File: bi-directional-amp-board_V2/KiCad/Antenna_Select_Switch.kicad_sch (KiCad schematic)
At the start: 17 parts

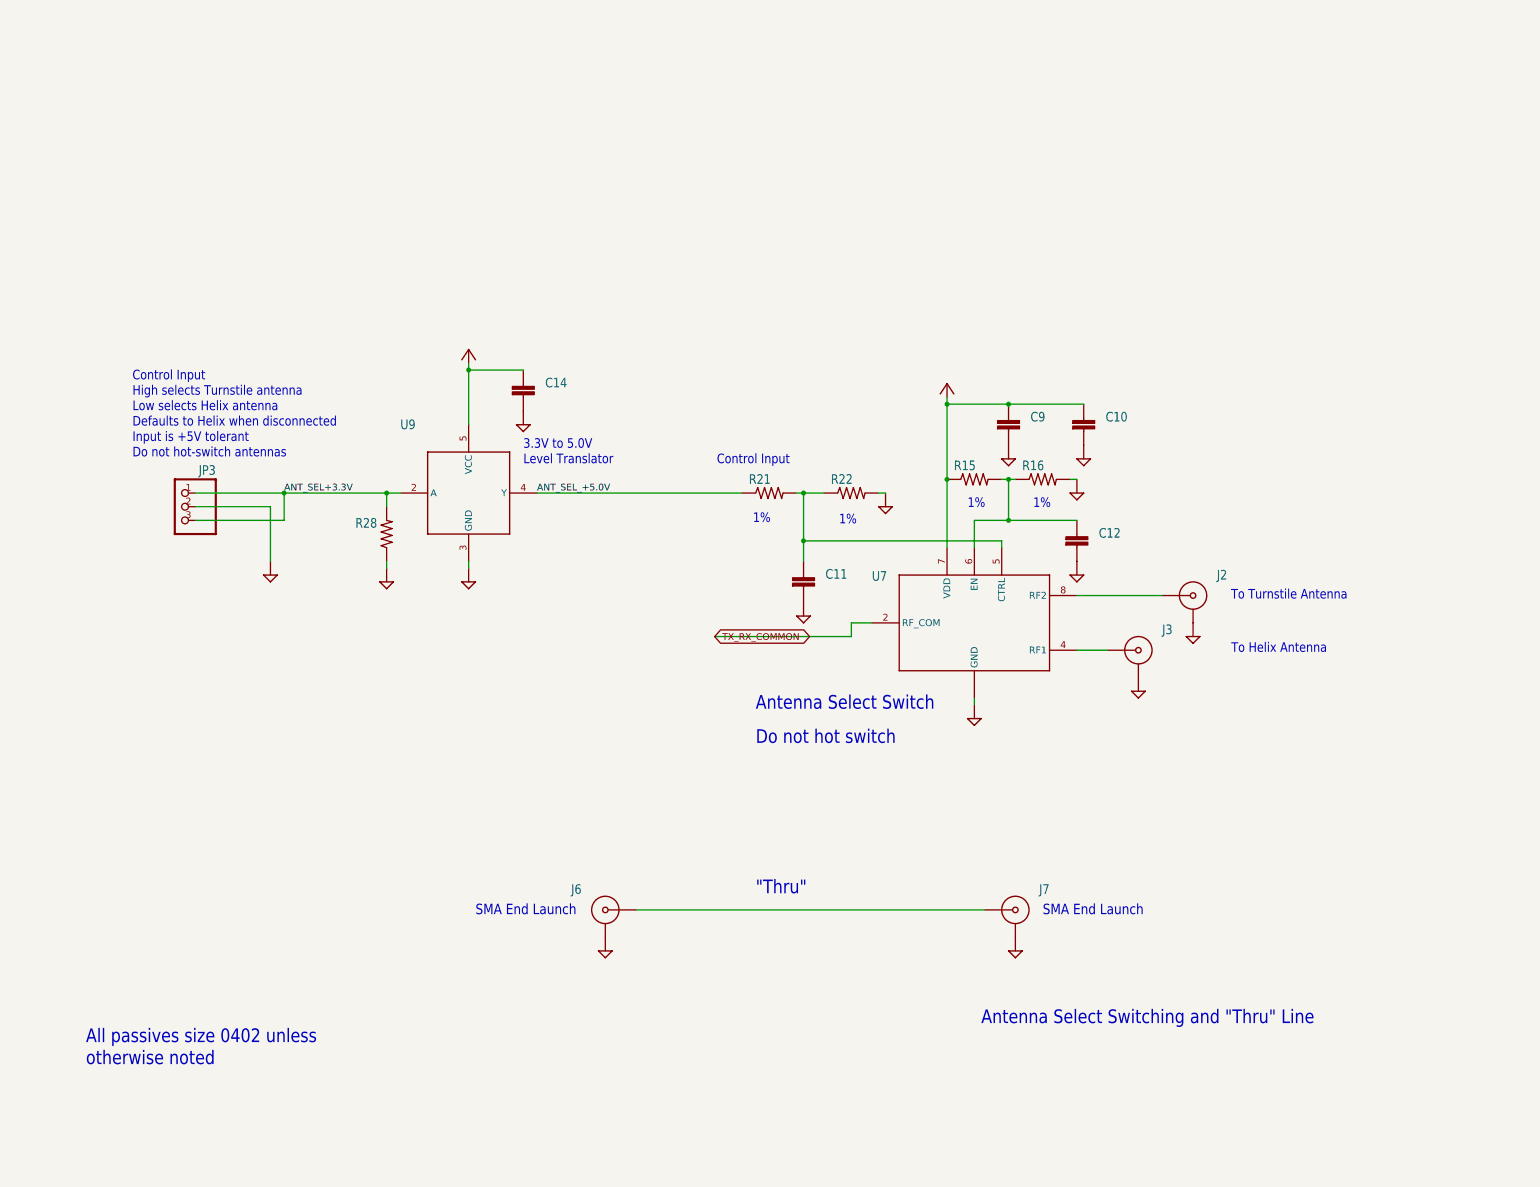
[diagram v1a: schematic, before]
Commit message: Updated KiCAD import of bidirectional amplifier. Still a bit broken, but better now.
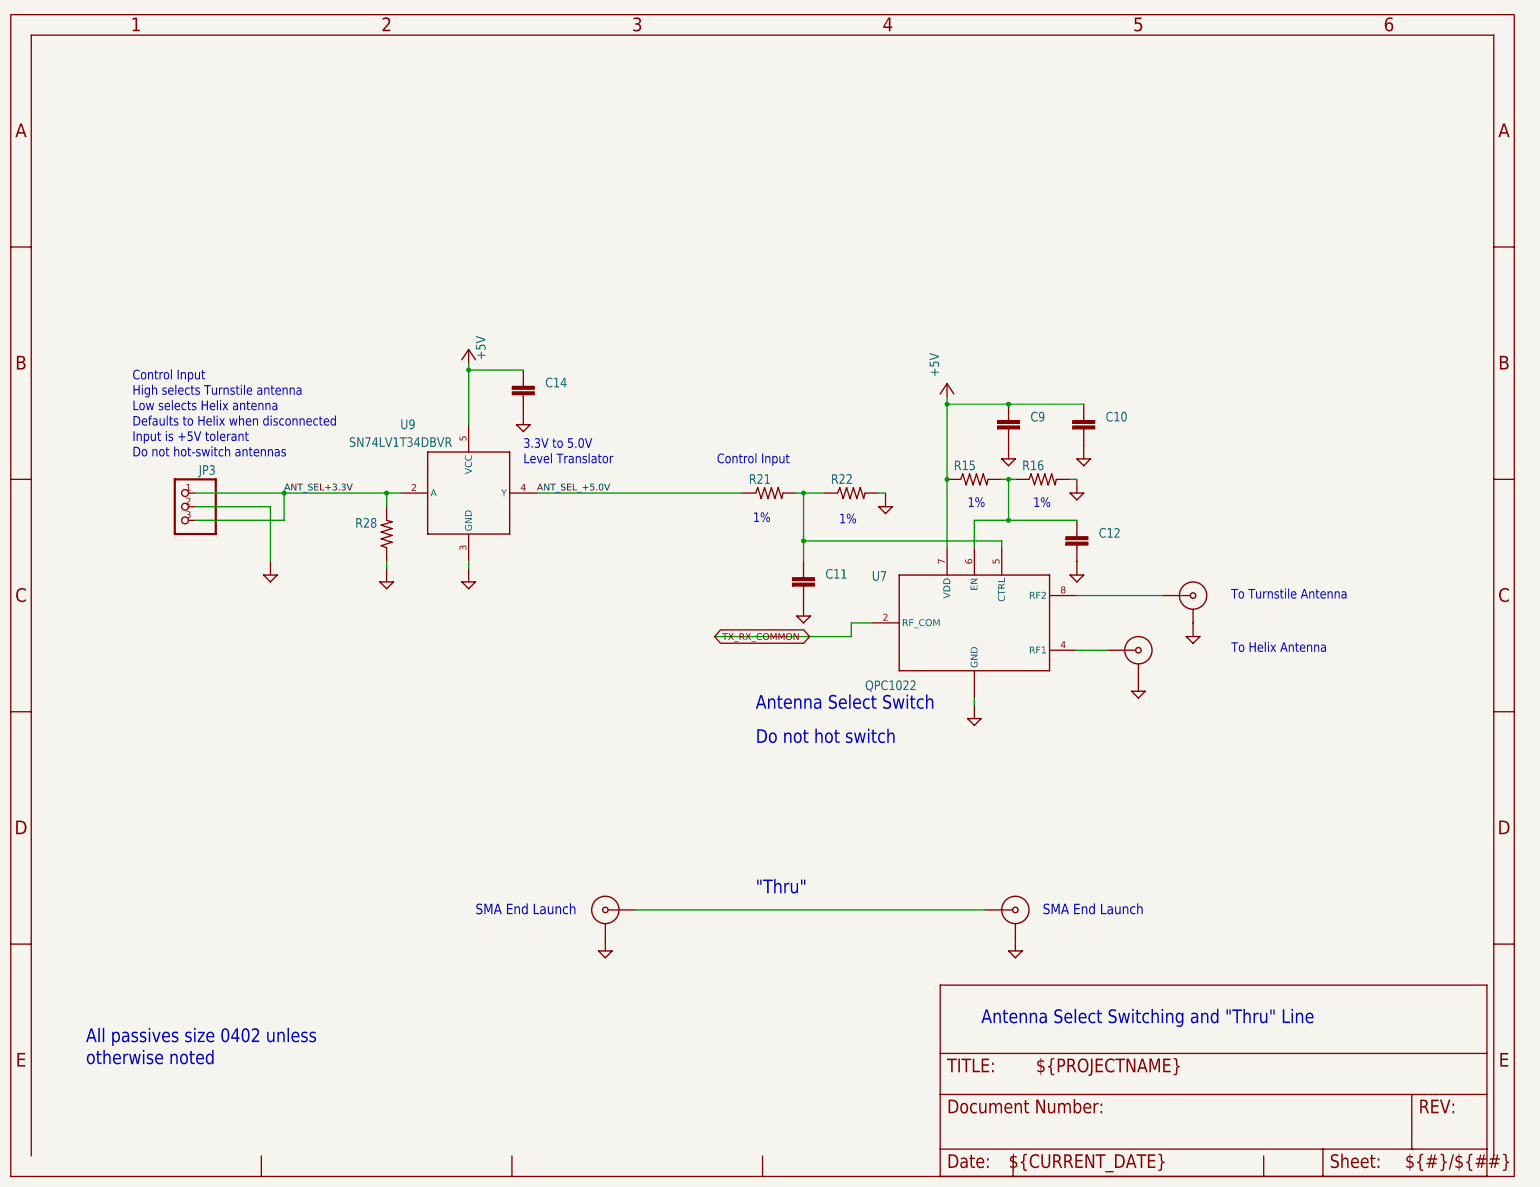
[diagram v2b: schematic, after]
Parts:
- C10, C14: value (none) -> C-EU0402-B-NOSILK; footprint (none) -> Bidirectional_Amp:.0402-B-NOSILK; MFR (none) -> TDK Corporation; MPN (none) -> CGA2B1X7R1C104K050BC
- C11, C12: value (none) -> C-EU0402-B-NOSILK; footprint (none) -> Bidirectional_Amp:.0402-B-NOSILK; MPN (none) -> GCM1555C1H101JA16D
- C9: value (none) -> C-EU0402-B-NOSILK; footprint (none) -> Bidirectional_Amp:.0402-B-NOSILK; MFR (none) -> Murata; MPN (none) -> GCM1555C1H101JA16D
- J2, J3, J6, J7: value (none) -> 142-0701-851_ALT; footprint (none) -> Bidirectional_Amp:142-0701-851; MFR (none) -> Cinch; MPN (none) -> 142-0701-851
- JP3: value (none) -> PINHD-1X3; footprint (none) -> Bidirectional_Amp:1X03; MFR (none) -> Molex; MPN (none) -> 22-23-2031
- R15, R21: value (none) -> R-US_0402-B-NOSILK; footprint (none) -> Bidirectional_Amp:.0402-B-NOSILK; MFR (none) -> Panasonic; MPN (none) -> ERJ-2RKF1002X
- R16, R22: value (none) -> R-US_0402-B-NOSILK; footprint (none) -> Bidirectional_Amp:.0402-B-NOSILK; MFR (none) -> Panasonic; MPN (none) -> ERJ-2RKF5621X
- R28: value (none) -> R-US_0402-B-NOSILK; footprint (none) -> Bidirectional_Amp:.0402-B-NOSILK; MFR (none) -> Panasonic; MPN (none) -> ERJ-2GEJ103X
- U7: value (none) -> QPC1022; footprint (none) -> Bidirectional_Amp:QPC1022
- U9: value (none) -> SN74LV1T34DBVR; footprint (none) -> Bidirectional_Amp:SOT95P280X145-5N
